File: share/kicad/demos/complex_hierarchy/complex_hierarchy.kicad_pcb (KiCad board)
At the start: 2 copper layers, 100.3 x 80 mm, 68 parts, among them P1 CONN_2, P2 CONN_2, P3 CONN_2, P4 CONN_2, P5 CONN_2, P6 CONN_2, Q1 MPAS92, Q2 MPAS42, Q3 MPAS92, Q4 MPAS42, Q5 MPAS92, Q6 MPAS42, Q7 MPAS92, Q8 MPAS42, U1 ICL7660, U2 78L05, U3 LM358N, U4 LM358N

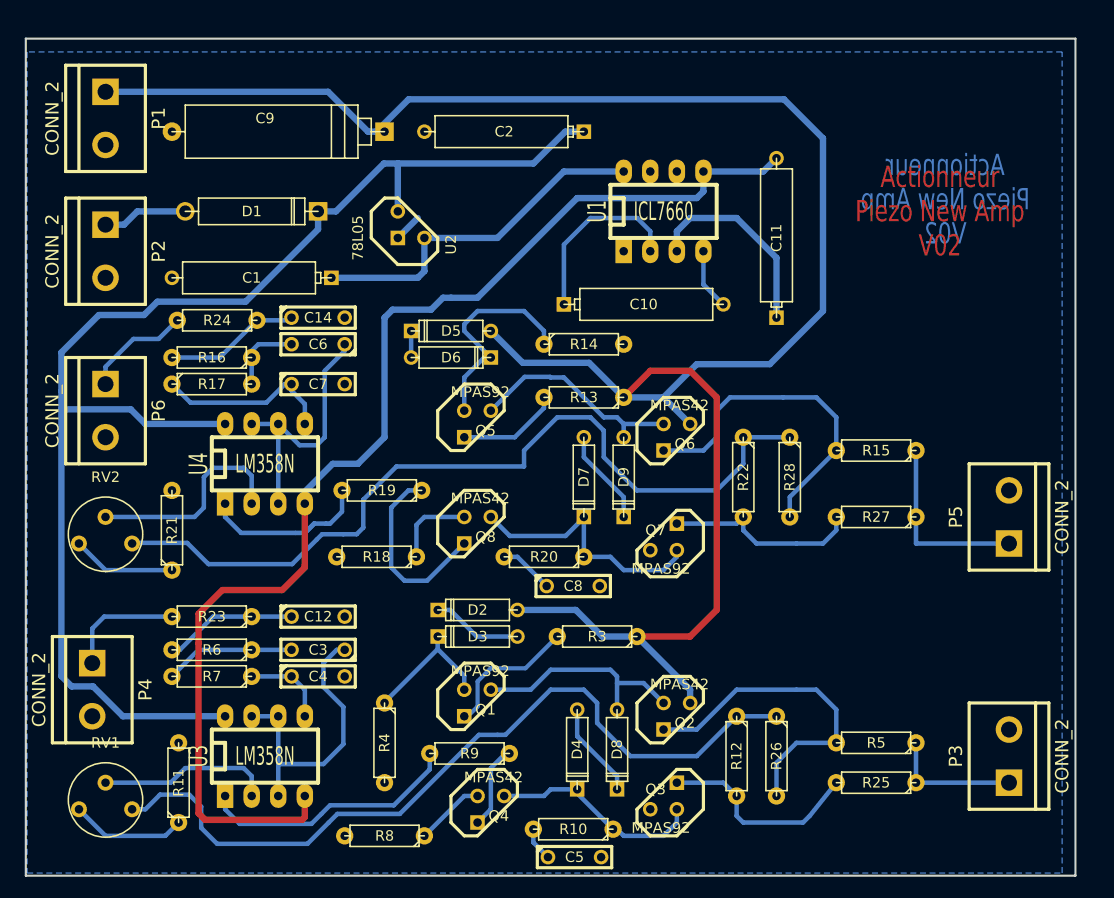
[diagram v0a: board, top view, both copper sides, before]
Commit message: Remove KiCad V4.0.7
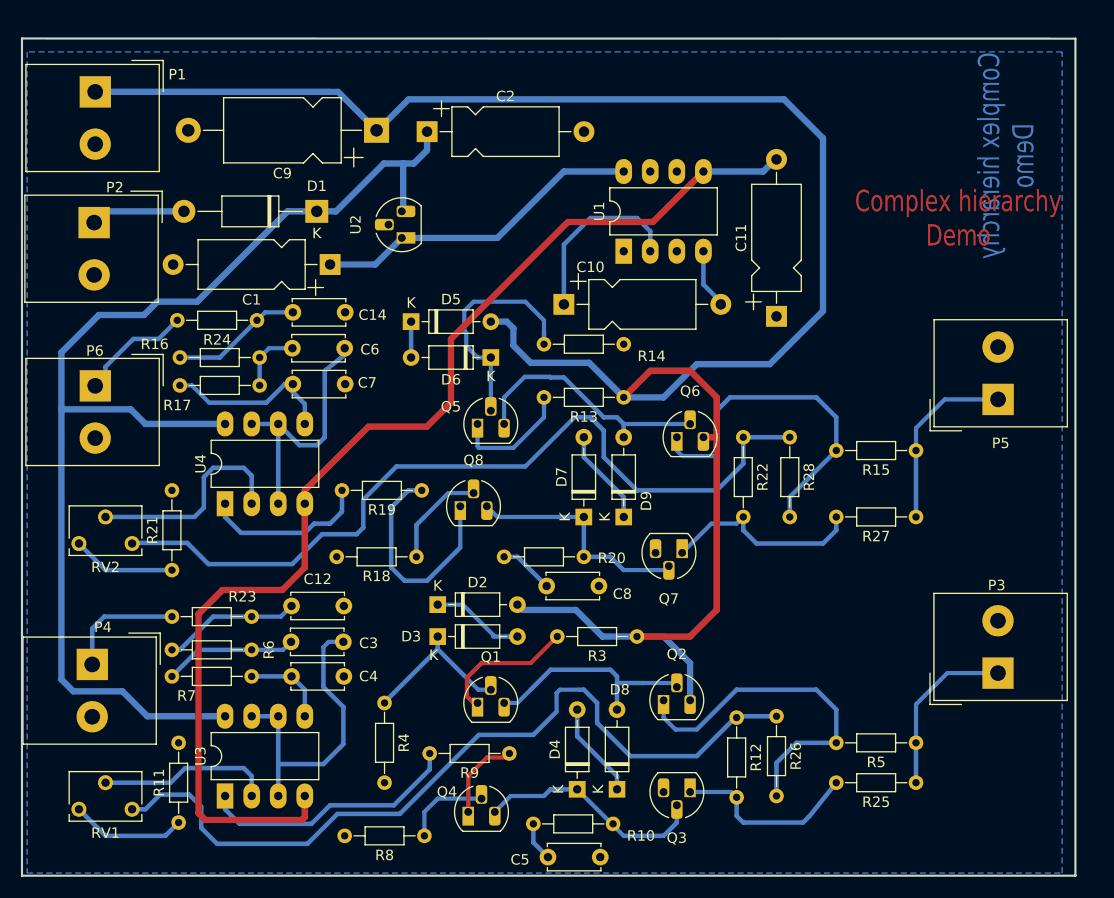
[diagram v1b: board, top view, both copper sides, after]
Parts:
- C1, C10, C11, C2: footprint discret:CP6 -> Capacitor_THT:CP_Axial_L10.0mm_D4.5mm_P15.00mm_Horizontal
- C12, C14, C3, C4, C5, C6, C7, C8: footprint discret:C2 -> Capacitor_THT:C_Disc_D5.0mm_W2.5mm_P5.00mm
- C9: footprint discret:CP8 -> Capacitor_THT:CP_Axial_L11.0mm_D6.0mm_P18.00mm_Horizontal
- D1: footprint discret:D5 -> Diode_THT:D_DO-41_SOD81_P12.70mm_Horizontal
- D2, D3, D4, D5, D6, D7, D8, D9: footprint discret:D3 -> Diode_THT:D_DO-35_SOD27_P7.62mm_Horizontal
- P1, P2, P3, P4, P5, P6: footprint connect:bornier2 -> TerminalBlock_Altech:Altech_AK300_1x02_P5.00mm_45-Degree
- Q1, Q3, Q5, Q7: value MPAS92 -> MPSA92; footprint discret:TO92-CBE -> Package_TO_SOT_THT:TO-92_HandSolder
- Q2, Q4, Q6, Q8: value MPAS42 -> MPSA42; footprint discret:TO92-CBE -> Package_TO_SOT_THT:TO-92_HandSolder
- R10, R11, R12, R13, R14, R15, R16, R17, R18, R19, R20, R21, R22, R23, R24, R25, R26, R27, R28, R3, R4, R5, R6, R7, R8, R9: footprint discret:R3-LARGE_PADS -> Resistor_THT:R_Axial_DIN0204_L3.6mm_D1.6mm_P7.62mm_Horizontal
- RV1, RV2: footprint discret:RV2 -> Potentiometer_THT:Potentiometer_Bourns_3266W_Vertical
- U1, U3, U4: footprint dip_sockets:DIP-8__300_ELL -> Package_DIP:DIP-8_W7.62mm_LongPads
- U2: footprint discret:LM78LXX -> Package_TO_SOT_THT:TO-92_HandSolder
- moved P5 11.3 mm to (181.2, 86.3)
- moved C9 9.40 mm to (121.8, 60.6)
- moved P3 8.01 mm to (181.2, 112.5)
- moved C10 7.62 mm to (139.7, 77.2)
- moved C1 7.60 mm to (117.3, 73.4)
- moved C11 7.49 mm to (160.0, 78.4)
- moved C2 7.37 mm to (126.6, 60.7), turned to 0 degrees
- moved D1 6.22 mm to (116.1, 68.3), turned to 180 degrees
- moved U1 5.39 mm to (145.4, 72.1), turned to 90 degrees
- moved U3 5.39 mm to (107.3, 124.2), turned to 90 degrees
- moved U4 5.39 mm to (107.3, 96.3), turned to 90 degrees
- moved R16 4.57 mm to (110.6, 82.3)
- moved D5 3.91 mm to (125.1, 78.9), turned to 0 degrees
- moved R10 3.84 mm to (144.4, 126.9)
- moved D2 3.84 mm to (127.6, 105.9), turned to 0 degrees
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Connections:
- R12 pad 2: Net-(Q3-PadE) -> Net-(Q3-Pad1)
- R13 pad 2: Net-(Q5-PadE) -> Net-(Q5-Pad1)
- R15 pad 2: Net-(Q6-PadE) -> Net-(Q6-Pad1)
- R18 pad 1: Net-(Q8-PadB) -> Net-(Q8-Pad2)
- R19 pad 1: Net-(Q8-PadE) -> Net-(Q8-Pad1)
- R22 pad 2: Net-(Q7-PadE) -> Net-(Q7-Pad1)
- R25 pad 2: Net-(Q3-PadE) -> Net-(Q3-Pad1)
- R26 pad 2: Net-(Q2-PadE) -> Net-(Q2-Pad1)
- R27 pad 2: Net-(Q7-PadE) -> Net-(Q7-Pad1)
- R28 pad 2: Net-(Q6-PadE) -> Net-(Q6-Pad1)
- R3 pad 2: Net-(Q1-PadE) -> Net-(Q1-Pad1)
- R5 pad 2: Net-(Q2-PadE) -> Net-(Q2-Pad1)
- R8 pad 1: Net-(Q4-PadB) -> Net-(Q4-Pad2)
- R9 pad 1: Net-(Q4-PadE) -> Net-(Q4-Pad1)
- U1 pad 6: Net-(U1-Pad6) -> unconnected-(U1-Pad6)
- U1 pad 7: Net-(U1-Pad7) -> unconnected-(U1-Pad7)
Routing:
- net Net-(Q2-Pad1): track 0.00 -> 33.9 mm
- net Net-(Q6-Pad1): track 0.00 -> 33.6 mm
- net Net-(Q6-PadE): track 32.3 -> 0.00 mm
- net Net-(Q2-PadE): track 31.7 -> 0.00 mm
- net GND: track 22.1 -> 0.00 mm
- net Net-(Q8-Pad1): track 0.00 -> 21.7 mm
- net Net-(Q7-Pad1): track 0.00 -> 19.7 mm
- net Net-(Q3-PadE): track 19.7 -> 0.00 mm
- net Net-(Q7-PadE): track 19.1 -> 0.00 mm
- net Net-(Q8-PadE): track 18.3 -> 0.00 mm
- net Net-(Q3-Pad1): track 0.00 -> 18.1 mm
- net +12V: track 128.7 -> 114.0 mm
- net Net-(Q1-PadE): track 13.5 -> 0.00 mm
- net Net-(Q1-Pad1): track 0.00 -> 13.3 mm
- net Net-(Q5-Pad1): track 0.00 -> 11.7 mm
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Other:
- board size 100.3 x 80 mm -> 100.7 x 80 mm
- net class Default removed
- net class power removed
- rule pad_to_mask_clearance: 0.254 -> 0
- board text added: "Complex hierarchy Demo"
- board text removed: "Actionneur Piezo New Amp V02"
